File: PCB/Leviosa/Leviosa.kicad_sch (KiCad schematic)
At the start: 48 parts, among them J1 JST servo 2, J2 JST Servo 1, J3 JST spare, Q3 TIP122, Q4 TIP122, U1 LM324, U2 ATtiny13A-P, U3 TPS1H200AQDGNRQ1, U5 L7805, U6 SS495A

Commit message: udpate footprints and schematic
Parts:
- SR206-TPCT-ND1: Link (none) -> https://jlcpcb.com/partdetail/DiodesIncorporated-B230A_13F/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
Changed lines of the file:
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@@
 			)
 		)
-		(property "Datasheet" "https://www.mccsemi.com/pdf/Products/SR202-SR2010(DO-41).pdf"
+		(property "Datasheet" "https://jlcpcb.com/api/file/downloadByFileSystemAccessId/8560078861175455744"
 			(at 243.84 55.88 0)
 			(effects
@@
 			)
 		)
+		(property "Link" "https://jlcpcb.com/partdetail/DiodesIncorporated-B230A_13F/C12889"
+			(at 243.84 55.88 90)
+			(effects
+				(font
+					(size 1.27 1.27)
+				)
+				(hide yes)
+			)
+		)

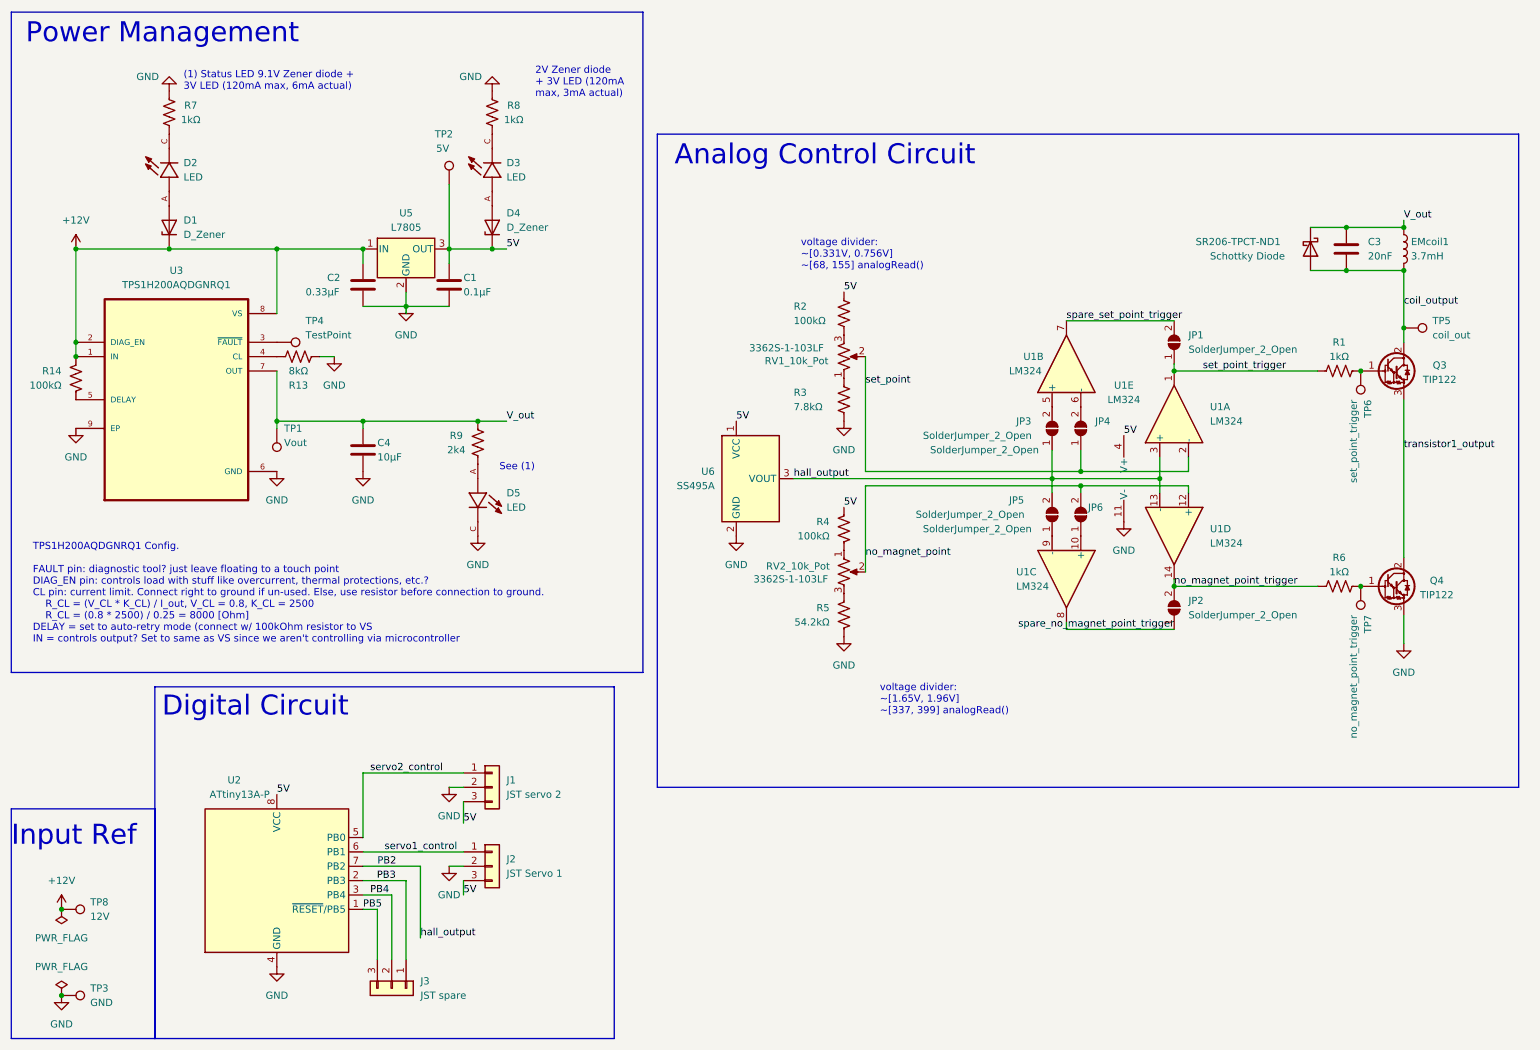
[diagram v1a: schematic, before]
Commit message: update diode footprint
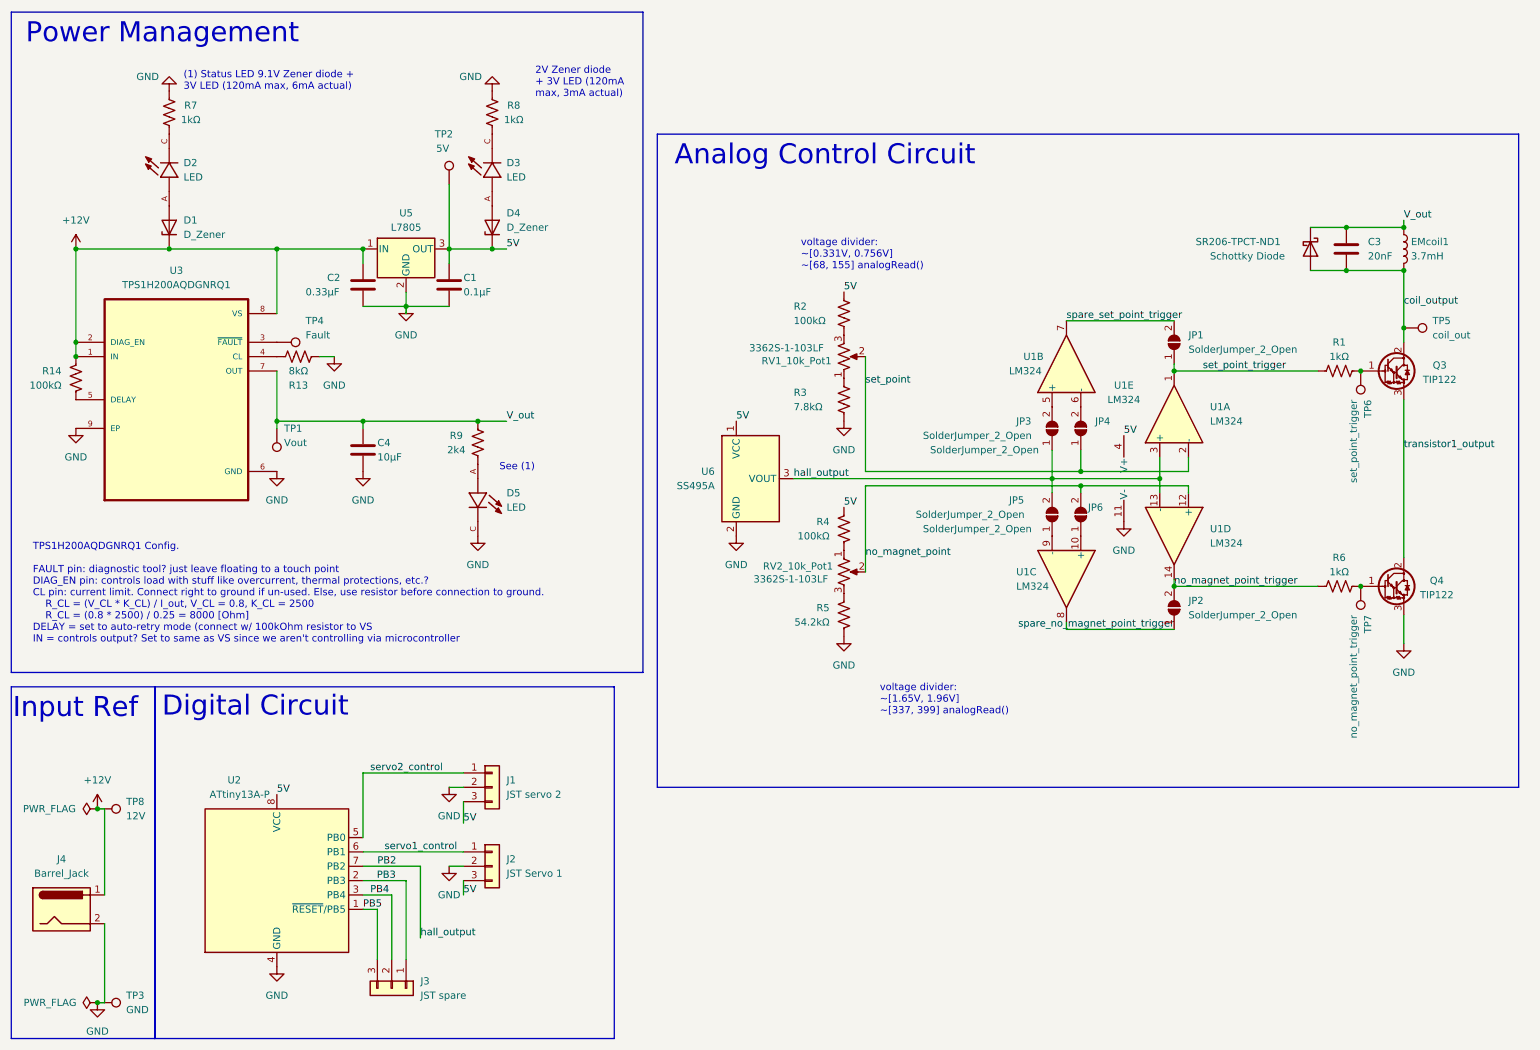
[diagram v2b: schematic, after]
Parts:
- added J4: Barrel_Jack, Connector_BarrelJack:BarrelJack_GCT_DCJ200-10-A_Horizontal, symbol Connector:Barrel_Jack
- RV2_10k_Pot1: renamed from RV2_10k_Pot; footprint Potentiometer_THT:Potentiometer_Alps_RK163_Single_Horizontal -> Potentiometer_THT:Potentiometer_ACP_CA6-H2,5_Horizontal
- SR206-TPCT-ND1: footprint Diode_THT:D_5KPW_P7.62mm_Vertical_AnodeUp -> B230A_13_F:SMA_DIO
- TP4: value TestPoint -> Fault
- renumbered RV1_10k_Pot to RV1_10k_Pot1
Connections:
- net +12V: now also J4.1
- net GND: now also J4.2
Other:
- moved on the sheet: TP3, TP8
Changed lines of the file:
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@@
 	)
 	(rectangle
-		(start 13.97 154.94)
+		(start 13.97 133.35)
 		(end 39.37 195.58)
 		(stroke
@@
 	(text "Input Ref"
 		(exclude_from_sim no)
-		(at 13.97 161.798 0)
+		(at 14.224 139.192 0)
 		(effects
 			(font
@@
 	)
 	(junction
-		(at 22.86 172.72)
+		(at 29.21 154.94)
 		(diameter 0)
 		(color 0 0 0 0)
@@
 	)
 	(junction
-		(at 22.86 187.96)
+		(at 29.21 189.23)
 		(diameter 0)
 		(color 0 0 0 0)
@@
 	(wire
 		(pts
+			(xy 30.48 175.26) (xy 30.48 189.23)
+		)
+		(stroke
+			(width 0)
+			(type default)
+		)
+	)
+	(wire
+		(pts
 			(xy 203.2 91.44) (xy 203.2 95.25)
 		)
@@
 	(wire
 		(pts
+			(xy 30.48 170.18) (xy 30.48 154.94)
+		)
+		(stroke
+			(width 0)
+			(type default)
+		)
+	)
+	(wire
+		(pts
 			(xy 41.91 55.88) (xy 60.96 55.88)
 		)
@@
 	(wire
 		(pts
+			(xy 29.21 189.23) (xy 30.48 189.23)
+		)
+		(stroke
+			(width 0)
+			(type default)
+		)
+	)
+	(wire
+		(pts
 			(xy 260.35 52.07) (xy 250.19 52.07)
 		)
@@
 	(wire
 		(pts
+			(xy 30.48 154.94) (xy 29.21 154.94)
+		)
+		(stroke
+			(width 0)
+			(type default)
+		)
+	)
+	(wire
+		(pts
 			(xy 78.74 172.72) (xy 78.74 181.61)
 		)
@@
 	)
 	(symbol
+		(lib_id "Connector:Barrel_Jack")
+		(at 22.86 172.72 0)
+		(unit 1)
+		(exclude_from_sim no)
+		(in_bom yes)
+		(on_board yes)
+		(dnp no)
+		(fields_autoplaced yes)
+		(property "Reference" "J4"
+			(at 22.86 163.83 0)
+			(effects
+				(font
+					(size 1.27 1.27)
+				)
+			)
+		)
+		(property "Value" "Barrel_Jack"
+			(at 22.86 166.37 0)
+			(effects
+				(font
+					(size 1.27 1.27)
+				)
+			)
+		)
+		(property "Footprint" "Connector_BarrelJack:BarrelJack_GCT_DCJ200-10-A_Horizontal"
+			(at 24.13 173.736 0)
+			(effects
+				(font
+					(size 1.27 1.27)
+				)
+				(hide yes)
+			)
+		)
+		(property "Datasheet" "~"
+			(at 24.13 173.736 0)
+			(effects
+				(font
+					(size 1.27 1.27)
+				)
+				(hide yes)
+			)
+		)
+		(property "Description" "DC Barrel Jack"
+			(at 22.86 172.72 0)
+			(effects
+				(font
+					(size 1.27 1.27)
+				)
+				(hide yes)
+			)
+		)
+		(pin "1"
+		)
+		(pin "2"
+		)
+		(instances
+			(project ""
+				(path "/fe766911-203b-467c-b704-d4bd488f6c98"
+					(reference "J4")
+					(unit 1)
+				)
+			)
+		)
+	)
+	(symbol
 		(lib_id "Device:R_Potentiometer_US")
 		(at 161.29 113.03 0)
@@
 		(on_board yes)
 		(dnp no)
-		(property "Reference" "RV2_10k_Pot"
+		(property "Reference" "RV2_10k_Pot1"
 			(at 153.162 112.014 0)
 			(effects
@@
 			)
 		)
-		(property "Footprint" "Potentiometer_THT:Potentiometer_Alps_RK163_Single_Horizontal"
+		(property "Footprint" "Potentiometer_THT:Potentiometer_ACP_CA6-H2,5_Horizontal"
 			(at 161.29 113.03 0)
 			(effects
@@
 			(project "Leviosa"
 				(path "/fe766911-203b-467c-b704-d4bd488f6c98"
-					(reference "RV2_10k_Pot")
+					(reference "RV2_10k_Pot1")
 					(unit 1)
 				)
@@
 			)
 		)
-		(property "Footprint" "Diode_THT:D_5KPW_P7.62mm_Vertical_AnodeUp"
+		(property "Footprint" "B230A_13_F:SMA_DIO"
 			(at 243.84 55.88 0)
 			(effects
@@
 	(symbol
 		(lib_id "Connector:TestPoint")
-		(at 22.86 187.96 270)
+		(at 29.21 189.23 270)
 		(unit 1)
 		(exclude_from_sim no)
@@
 		(fields_autoplaced yes)
 		(property "Reference" "TP3"
-			(at 27.94 186.6899 90)
+			(at 34.29 187.9599 90)
 			(effects
 				(font
@@
 		)
 		(property "Value" "GND"
-			(at 27.94 189.2299 90)
+			(at 34.29 190.4999 90)
 			(effects
 				(font
@@
 		)
 		(property "Footprint" "TestPoint:TestPoint_Pad_D3.0mm"
-			(at 22.86 193.04 0)
+			(at 29.21 194.31 0)
 			(effects
 				(font
@@
 		)
 		(property "Datasheet" "~"
-			(at 22.86 193.04 0)
+			(at 29.21 194.31 0)
 			(effects
 				(font
@@
 		)
 		(property "Description" ""
-			(at 22.86 187.96 0)
+			(at 29.21 189.23 0)
 			(effects
 				(font
@@
 	(symbol
 		(lib_id "power:GND")
-		(at 22.86 187.96 0)
+		(at 29.21 189.23 0)
 		(unit 1)
 		(exclude_from_sim no)
@@
 		(fields_autoplaced yes)
 		(property "Reference" "#PWR06"
-			(at 22.86 194.31 0)
+			(at 29.21 195.58 0)
 			(effects
 				(font
@@
 		)
 		(property "Value" "GND"
-			(at 22.86 193.04 0)
+			(at 29.21 194.31 0)
 			(effects
 				(font
@@
 		)
 		(property "Footprint" "Connector_Pin:Pin_D1.0mm_L10.0mm"
-			(at 22.86 187.96 0)
+			(at 29.21 189.23 0)
 			(effects
 				(font
@@
 		)
 		(property "Datasheet" ""
-			(at 22.86 187.96 0)
+			(at 29.21 189.23 0)
 			(effects
 				(font
@@
 		)
 		(property "Description" ""
-			(at 22.86 187.96 0)
+			(at 29.21 189.23 0)
 			(effects
 				(font
@@
 	(symbol
 		(lib_id "power:+12V")
-		(at 22.86 172.72 0)
+		(at 29.21 154.94 0)
 		(unit 1)
 		(exclude_from_sim no)
@@
 		(fields_autoplaced yes)
 		(property "Reference" "#PWR03"
-			(at 22.86 176.53 0)
+			(at 29.21 158.75 0)
 			(effects
 				(font
@@
 		)
 		(property "Value" "+12V"
-			(at 22.86 167.64 0)
+			(at 29.21 149.86 0)
 			(effects
 				(font
@@
 		)
 		(property "Footprint" "Connector_Pin:Pin_D1.0mm_L10.0mm"
-			(at 22.86 172.72 0)
+			(at 29.21 154.94 0)
 			(effects
 				(font
@@
 		)
 		(property "Datasheet" ""
-			(at 22.86 172.72 0)
+			(at 29.21 154.94 0)
 			(effects
 				(font
@@
 		)
 		(property "Description" ""
-			(at 22.86 172.72 0)
+			(at 29.21 154.94 0)
 			(effects
 				(font
@@
 	(symbol
 		(lib_id "power:PWR_FLAG")
-		(at 22.86 187.96 0)
-		(mirror y)
+		(at 29.21 189.23 90)
+		(mirror x)
 		(unit 1)
 		(exclude_from_sim no)
@@
 		(dnp no)
 		(property "Reference" "#FLG02"
-			(at 22.86 186.055 0)
+			(at 27.305 189.23 0)
 			(effects
 				(font
@@
 		)
 		(property "Value" "PWR_FLAG"
-			(at 22.86 182.88 0)
+			(at 20.828 189.23 90)
 			(effects
 				(font
@@
 		)
 		(property "Footprint" ""
-			(at 22.86 187.96 0)
+			(at 29.21 189.23 0)
 			(effects
 				(font
@@
 		)
 		(property "Datasheet" "~"
-			(at 22.86 187.96 0)
+			(at 29.21 189.23 0)
 			(effects
 				(font
@@
 		)
 		(property "Description" ""
-			(at 22.86 187.96 0)
+			(at 29.21 189.23 0)
 			(effects
 				(font
@@
 			)
 		)
-		(property "Value" "TestPoint"
+		(property "Value" "Fault"
 			(at 66.04 71.12 90)
 			(effects
@@
 		(on_board yes)
 		(dnp no)
-		(property "Reference" "RV1_10k_Pot"
+		(property "Reference" "RV1_10k_Pot1"
 			(at 152.908 75.692 0)
 			(effects
@@
 			(project "Leviosa"
 				(path "/fe766911-203b-467c-b704-d4bd488f6c98"
-					(reference "RV1_10k_Pot")
+					(reference "RV1_10k_Pot1")
 					(unit 1)
 				)
@@
 	(symbol
 		(lib_id "Connector:TestPoint")
-		(at 22.86 172.72 270)
+		(at 29.21 154.94 270)
 		(unit 1)
 		(exclude_from_sim no)
@@
 		(fields_autoplaced yes)
 		(property "Reference" "TP8"
-			(at 27.94 171.4499 90)
+			(at 34.29 153.6699 90)
 			(effects
 				(font
@@
 		)
 		(property "Value" "12V"
-			(at 27.94 173.9899 90)
+			(at 34.29 156.2099 90)
 			(effects
 				(font
@@
 		)
 		(property "Footprint" "TestPoint:TestPoint_Pad_D3.0mm"
-			(at 22.86 177.8 0)
+			(at 29.21 160.02 0)
 			(effects
 				(font
@@
 		)
 		(property "Datasheet" "~"
-			(at 22.86 177.8 0)
+			(at 29.21 160.02 0)
 			(effects
 				(font
@@
 		)
 		(property "Description" ""
-			(at 22.86 172.72 0)
+			(at 29.21 154.94 0)
 			(effects
 				(font
@@
 	(symbol
 		(lib_id "power:PWR_FLAG")
-		(at 22.86 172.72 180)
+		(at 29.21 154.94 90)
 		(unit 1)
 		(exclude_from_sim no)
@@
 		(fields_autoplaced yes)
 		(property "Reference" "#FLG01"
-			(at 22.86 174.625 0)
+			(at 27.305 154.94 0)
 			(effects
 				(font
@@
 		)
 		(property "Value" "PWR_FLAG"
-			(at 22.86 177.8 0)
+			(at 25.4 154.9399 90)
 			(effects
 				(font
 					(size 1.27 1.27)
 				)
+				(justify left)
 			)
 		)
 		(property "Footprint" ""
-			(at 22.86 172.72 0)
+			(at 29.21 154.94 0)
 			(effects
 				(font
@@
 		)
 		(property "Datasheet" "~"
-			(at 22.86 172.72 0)
+			(at 29.21 154.94 0)
 			(effects
 				(font
@@
 		)
 		(property "Description" ""
-			(at 22.86 172.72 0)
+			(at 29.21 154.94 0)
 			(effects
 				(font

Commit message: chnagd resistors, didoes and connectors to horizontal common 2.54mm headers
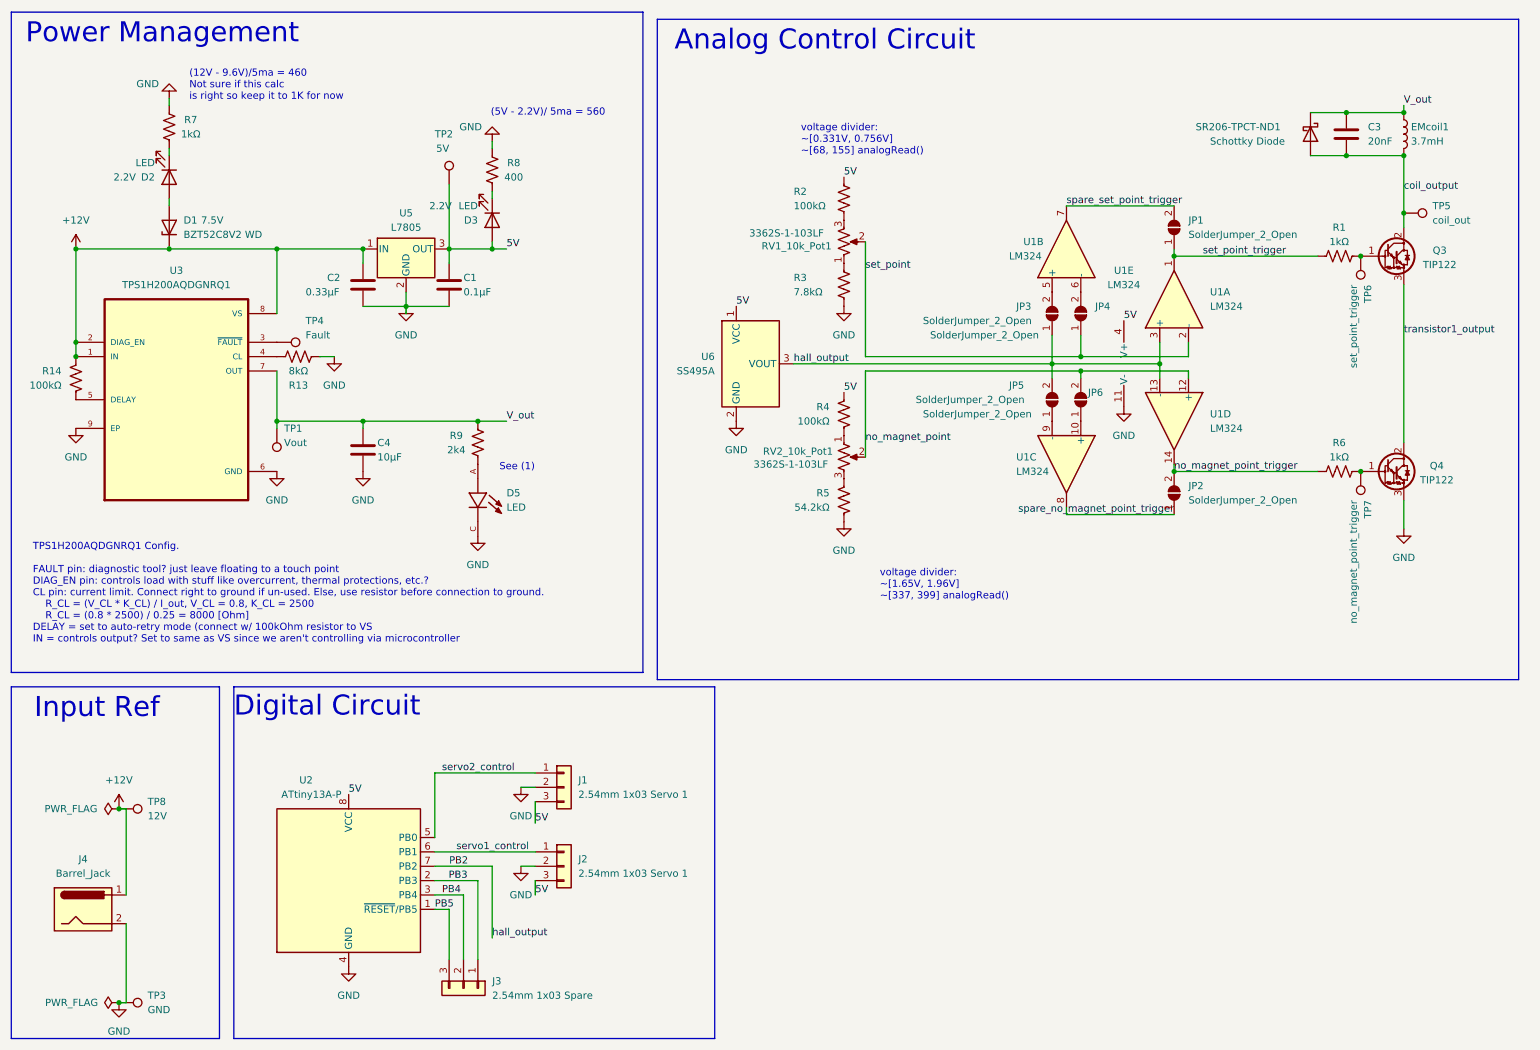
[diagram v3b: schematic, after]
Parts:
- removed D4: D_Zener, SZMMSZ4679T1G:SOD-123_ONS, symbol Device:D_Zener
- D1: value D_Zener -> BZT52C8V2 WD; footprint SMAZ9V1-13-F:SMA_DIO -> Diode_SMD:D_SOD-123; Vbr (none) -> 7.5V
- D2: symbol MP-2016-1100-50-70:MP-2016-1100-50-70 -> Device:LED; Vf (none) -> 2.2V
- D3: footprint MP-2016-1100-50-70:LED_MP-2016-1100-50-70 -> LED_SMD:LED_0805_2012Metric; symbol MP-2016-1100-50-70:MP-2016-1100-50-70 -> Device:LED; Vf (none) -> 2.2V
- J1: value JST servo 2 -> 2.54mm 1x03 Servo 1; footprint Connector_JST:JST_ACH_BM03B-ACHSS-GAN-ETF_1x03-1MP_P1.20mm_Vertical -> Connector_PinHeader_2.54mm:PinHeader_1x03_P2.54mm_Horizontal
- J2: value JST Servo 1 -> 2.54mm 1x03 Servo 1; footprint Connector_JST:JST_ACH_BM03B-ACHSS-GAN-ETF_1x03-1MP_P1.20mm_Vertical -> Connector_PinHeader_2.54mm:PinHeader_1x03_P2.54mm_Horizontal
- J3: value JST spare -> 2.54mm 1x03 Spare; footprint Connector_JST:JST_ACH_BM03B-ACHSS-GAN-ETF_1x03-1MP_P1.20mm_Vertical -> Connector_PinHeader_2.54mm:PinHeader_1x03_P2.54mm_Horizontal
- J4: footprint Connector_BarrelJack:BarrelJack_GCT_DCJ200-10-A_Horizontal -> Connector_BarrelJack:BarrelJack_Kycon_KLDX-0202-xC_Horizontal
- R8: value 1kΩ -> 400
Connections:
- net 5V: now also D3.2 (A)
- net at R7.1: now also D2.1 (K); no longer D2.C
- net at R8.1: now also D3.1 (K); no longer D3.C
- net at D1.2 (A): now also D2.2 (A); no longer D2.A
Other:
- note added: "(12V - 9.6V)/5ma = 460 Not sure if this calc is right so keep it to 1K for now"
- note added: "(5V - 2.2V)/ 5ma = 560"
- note removed: "(1) Status LED 9.1V Zener diode + 3V LED (120mA max, 6mA actual)"
- note removed: "2V Zener diode + 3V LED (120mA max, 3mA actual)"
- moved on the sheet: C3, EMcoil1, J1, J2, J3, J4, JP1, JP2, JP3, JP4, JP5, JP6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
